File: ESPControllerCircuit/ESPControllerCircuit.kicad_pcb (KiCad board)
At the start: 2 copper layers, 5 parts, among them J1 Conn_01x02_Female, SW1 SW_Push, U1 WeMos_mini

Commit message: Basic controller circuit
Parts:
- removed J1: Conn_01x02_Female, Pin_Headers:Pin_Header_Straight_1x02_Pitch2.54mm
- added DEBUG1: Conn_01x02_Female, Pin_Headers:Pin_Header_Straight_1x02_Pitch2.54mm, F.Cu at (142.5, 137.8)
- added R2: 470R, Resistors_SMD:R_0805_HandSoldering, F.Cu at (131.8, 152.8)
- added R3: 220R, Resistors_SMD:R_0805_HandSoldering, F.Cu at (120.2, 152.8)
- added REF**: MountingHole_2.5mm, Mounting_Holes:MountingHole_2.5mm, F.Cu at (103.0, 110.0)
- added REF**: MountingHole_2.5mm, Mounting_Holes:MountingHole_2.5mm, F.Cu at (145.0, 110.0)
- added REF**: MountingHole_2.5mm, Mounting_Holes:MountingHole_2.5mm, F.Cu at (145.0, 64.0)
- added REF**: MountingHole_2.5mm, Mounting_Holes:MountingHole_2.5mm, F.Cu at (103.0, 64.0)
- added REF**: MountingHole_2.5mm, Mounting_Holes:MountingHole_2.5mm, F.Cu at (103.0, 157.0)
- added REF**: MountingHole_2.5mm, Mounting_Holes:MountingHole_2.5mm, F.Cu at (145.0, 157.0)
- added RX1: Conn_01x02_Male, Connectors_JST:JST_PH_S2B-PH-K_02x2.00mm_Angled, F.Cu at (137.0, 153.2)
- added TX1: Conn_01x02_Male, Connectors_JST:JST_PH_S2B-PH-K_02x2.00mm_Angled, F.Cu at (109.0, 153.2)
- added U2: HMHA2801, Housings_SSOP:SOP-4_4.4x2.8mm_Pitch1.27mm, F.Cu at (115.8, 155.5)
- D1: value LED -> COMMS
- R1: value 512R -> 470R
- moved R1 42.8 mm to (107.8, 147.0)
- moved D1 42.5 mm to (102.8, 147.0)
- moved U1 30.0 mm to (124.2, 132.2)
- moved SW1 19.4 mm to (145.5, 117.0), turned to 270 degrees
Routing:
- net +3V3: track 0.00 -> 33.1 mm
- net Net-(R2-Pad2): track 0.00 -> 31.8 mm
- net Net-(R3-Pad2): track 0.00 -> 17.8 mm
- net Net-(R1-Pad2): track 0.00 -> 15.8 mm
- net Net-(SW1-Pad2): track 0.00 -> 13.9 mm
- net Net-(TX1-Pad1): track 0.00 -> 8.99 mm
- net Net-(DEBUG1-Pad1): track 0.00 -> 8.12 mm
- net Net-(TX1-Pad2): track 0.00 -> 8.07 mm
- net Net-(R3-Pad1): track 0.00 -> 2.68 mm
- net Net-(D1-Pad2): track 0.00 -> 2.30 mm
- net GND: vias 0 -> 10
- added copper zone on B.Cu, net GND
- added copper zone on F.Cu, net GND
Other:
- board outline added: 48 x 99 mm

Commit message: End of day checkin
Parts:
- added R4: 10K, Resistors_SMD:R_0805_HandSoldering, F.Cu at (130.5, 128.2)
- added R5: 10K, Resistors_SMD:R_0805_HandSoldering, F.Cu at (130.5, 131.1)
- added U3: PCF8574AT/3 - I/O Expander, 8bit, 100 kHz, I2C, SMD_Packages:SO-16-W, F.Cu at (125.0, 118.8)
- R2: value 470R -> 4K7
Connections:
- U1 pad 11: Net-(U1-Pad11) -> Net-(R1-Pad2)
- U1 pad 12: Net-(U1-Pad12) -> PCFINT
- U1 pad 13: Net-(R1-Pad2) -> Net-(U1-Pad13)
- U1 pad 4: Net-(U1-Pad4) -> Net-(SW1-Pad2)
- U1 pad 5: Net-(U1-Pad5) -> SCL
- U1 pad 6: Net-(SW1-Pad2) -> SDA
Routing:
- net +3V3: track 33.1 -> 63.3 mm, vias 0 -> 1
- net SCL: track 0.00 -> 16.8 mm
- net PCFINT: track 0.00 -> 16.0 mm
- net SDA: track 0.00 -> 12.6 mm
- net Net-(R2-Pad2): track 31.8 -> 39.3 mm
- net Net-(SW1-Pad2): track 13.9 -> 20.8 mm
- net Net-(R1-Pad2): track 15.8 -> 21.6 mm
- net GND: track 0.00 -> 2.54 mm, vias 10 -> 20

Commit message: Got i2c working for PCF8574 chip
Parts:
- R4, R5: value 10K -> 4K7
- U3: value PCF8574AT/3 - I/O Expander, 8bit, 100 kHz, I2C -> PCF8574AT/3
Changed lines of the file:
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@@
       (effects (font (size 1 1) (thickness 0.15)))
     )
-    (fp_text value "PCF8574AT/3 -  I/O Expander, 8bit, 100 kHz, I2C" (at -39.75 3.75 180) (layer F.Fab)
+    (fp_text value PCF8574AT/3 (at -0.25 -2.75 180) (layer F.Fab)
       (effects (font (size 1 1) (thickness 0.15)))
     )
@@
       (effects (font (size 1 1) (thickness 0.15)))
     )
-    (fp_text value 10K (at 0 1.75) (layer F.Fab)
+    (fp_text value 4K7 (at 0 1.75) (layer F.Fab)
       (effects (font (size 1 1) (thickness 0.15)))
     )
@@
       (effects (font (size 1 1) (thickness 0.15)))
     )
-    (fp_text value 10K (at 0 1.75) (layer F.Fab)
+    (fp_text value 4K7 (at 0 1.75) (layer F.Fab)
       (effects (font (size 1 1) (thickness 0.15)))
     )
@@
       (effects (font (size 1 1) (thickness 0.15)))
     )
-    (fp_text value WeMos_mini (at 15.25 -7.75) (layer F.Fab)
-      (effects (font (size 1 1) (thickness 0.15)))
-    )
+    (fp_text value WeMos_mini (at -2.25 -8.25 90) (layer F.Fab)
+      (effects (font (size 1 1) (thickness 0.15)))
+    )

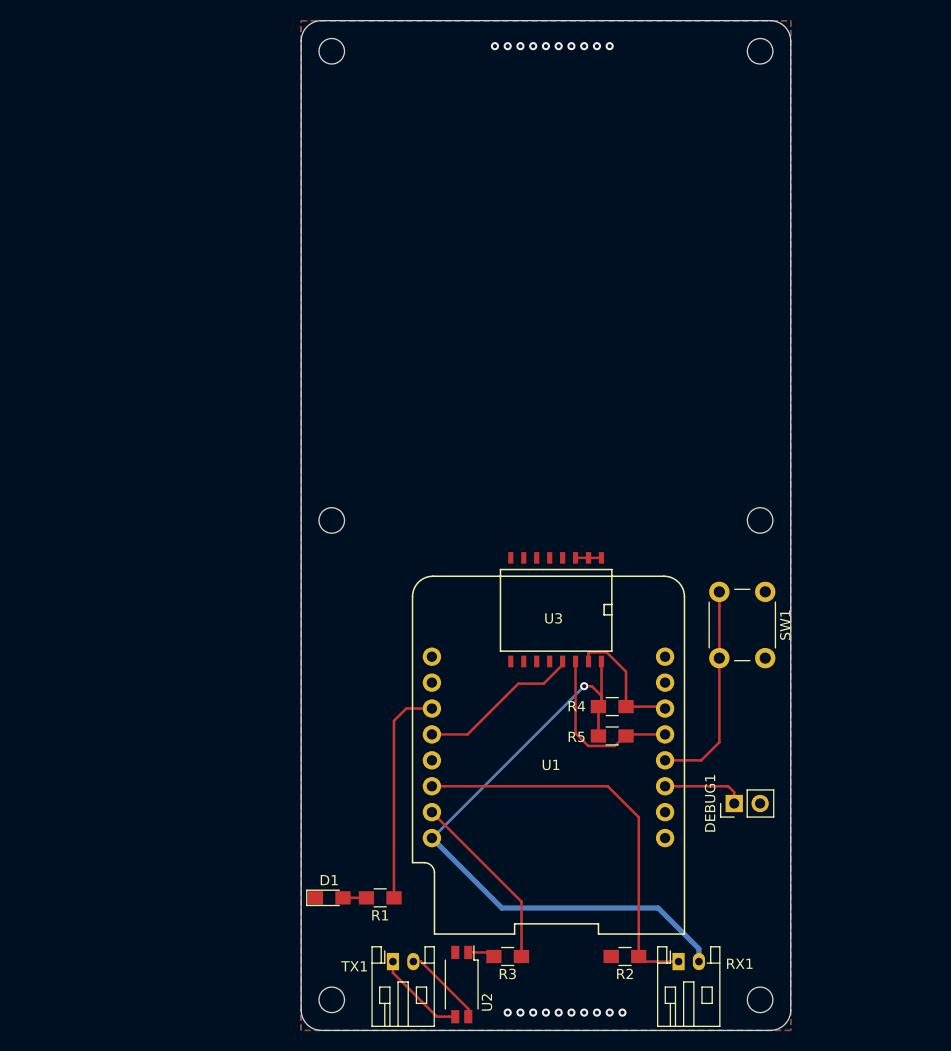
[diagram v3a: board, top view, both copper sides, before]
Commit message: Controller module PCB design
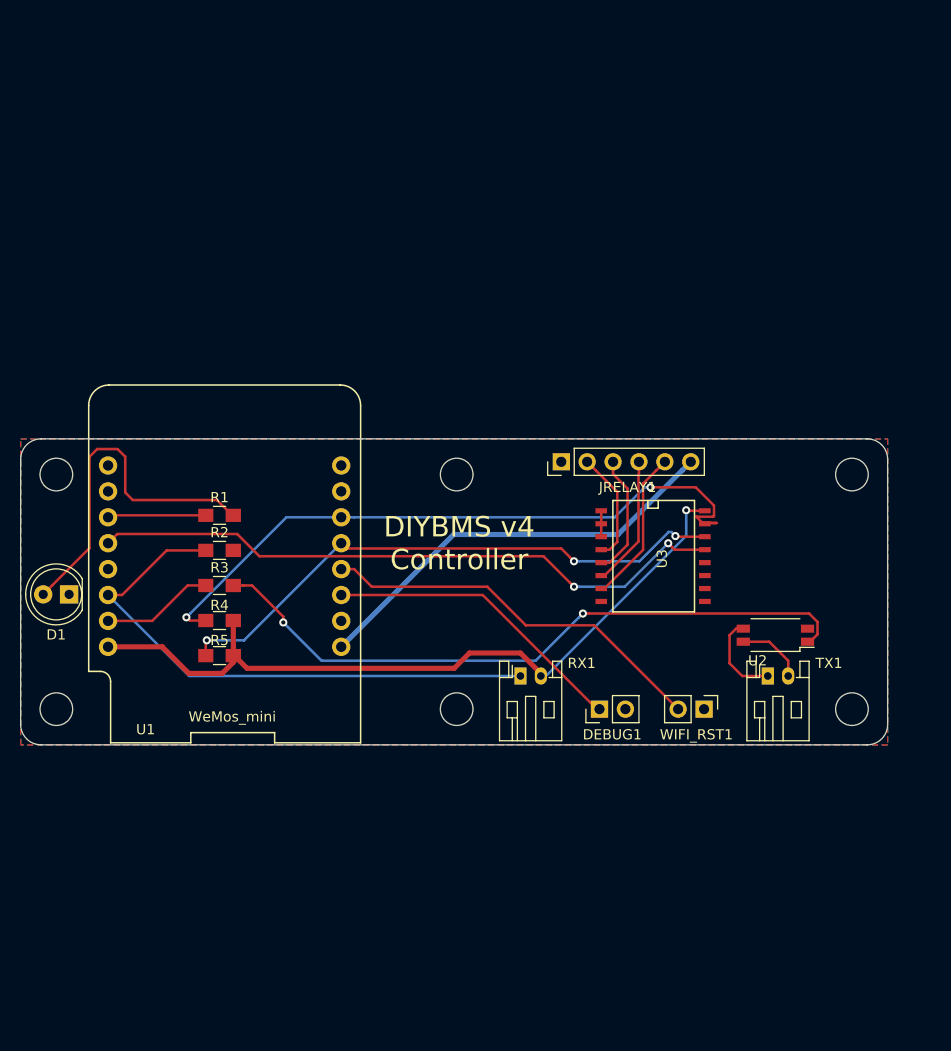
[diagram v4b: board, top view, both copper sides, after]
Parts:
- removed the REF** at (103.0, 110.0)
- removed the REF** at (145.0, 110.0)
- removed the REF** at (145.0, 64.0)
- removed the REF** at (103.0, 64.0)
- removed the REF** at (103.0, 157.0)
- removed the REF** at (145.0, 157.0)
- removed SW1: SW_Push, Buttons_Switches_THT:SW_PUSH_6mm
- added JRELAY1: Conn_01x06_Male, Pin_Headers:Pin_Header_Straight_1x06_Pitch2.54mm, F.Cu at (125.5, 104.2)
- added REF**: MountingHole_3.2mm_M3, Mounting_Holes:MountingHole_3.2mm_M3, F.Cu at (115.2, 128.5)
- added REF**: MountingHole_3.2mm_M3, Mounting_Holes:MountingHole_3.2mm_M3, F.Cu at (115.2, 105.5)
- added REF**: MountingHole_3.2mm_M3, Mounting_Holes:MountingHole_3.2mm_M3, F.Cu at (76.0, 105.5)
- added REF**: MountingHole_3.2mm_M3, Mounting_Holes:MountingHole_3.2mm_M3, F.Cu at (76.0, 128.5)
- added REF**: MountingHole_3.2mm_M3, Mounting_Holes:MountingHole_3.2mm_M3, F.Cu at (154.0, 128.5)
- added REF**: MountingHole_3.2mm_M3, Mounting_Holes:MountingHole_3.2mm_M3, F.Cu at (154.0, 105.5)
- added WIFI_RST1: WIFI RST, Pin_Headers:Pin_Header_Straight_1x02_Pitch2.54mm, F.Cu at (139.5, 128.5)
- D1: footprint LEDs:LED_0805_HandSoldering -> LEDs:LED_D5.0mm
- moved R2 56.3 mm to (92.0, 112.9), turned to 180 degrees
- moved TX1 46.2 mm to (145.8, 125.2)
- moved R3 46.1 mm to (92.0, 116.4), turned to 180 degrees
- moved U2 46.0 mm to (146.5, 121.2), turned to 180 degrees
- moved R1 40.7 mm to (92.0, 109.5), turned to 180 degrees
- moved R4 39.4 mm to (92.0, 119.8), turned to 180 degrees
- moved R5 39.3 mm to (92.0, 123.2), turned to 180 degrees
- moved D1 39.2 mm to (77.2, 117.2), turned to 180 degrees
- moved U1 36.9 mm to (92.5, 113.5)
- moved RX1 32.0 mm to (121.5, 125.2)
- moved DEBUG1 16.1 mm to (129.2, 128.5)
- moved U3 10.9 mm to (134.5, 113.5), turned to 270 degrees
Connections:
- U1 pad 10: Net-(U1-Pad10) -> (no net)
- U1 pad 13: Net-(U1-Pad13) -> (no net)
- U1 pad 7: Net-(U1-Pad7) -> (no net)
- U1 pad 8: Net-(U1-Pad8) -> (no net)
- U1 pad 9: Net-(U1-Pad9) -> (no net)
- U3 pad 10: Net-(U3-Pad10) -> (no net)
- U3 pad 11: Net-(U3-Pad11) -> (no net)
- U3 pad 12: Net-(U3-Pad12) -> (no net)
- U3 pad 9: Net-(U3-Pad9) -> (no net)
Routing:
- net Net-(R3-Pad1): track 2.68 -> 65.4 mm, vias 0 -> 2
- net SDA: track 12.6 -> 66.0 mm, vias 0 -> 2
- net PCFINT: track 16.0 -> 63.0 mm, vias 0 -> 2
- net +5V: track 0.00 -> 41.8 mm
- net SCL: track 16.8 -> 56.4 mm, vias 0 -> 3
- net Net-(D1-Pad2): track 2.30 -> 34.5 mm
- net Net-(DEBUG1-Pad1): track 8.12 -> 30.0 mm
- net Net-(U1-Pad4): track 20.8 -> 38.7 mm
- net Net-(R2-Pad2): track 39.3 -> 55.1 mm
- net Net-(JRELAY1-Pad5): track 0.00 -> 15.2 mm
- net Net-(JRELAY1-Pad4): track 0.00 -> 12.9 mm
- net Net-(JRELAY1-Pad3): track 0.00 -> 12.0 mm
- net Net-(R1-Pad2): track 21.6 -> 9.66 mm
- net +3V3: track 63.3 -> 74.6 mm
- net Net-(JRELAY1-Pad2): track 0.00 -> 11.0 mm
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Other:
- board size 48 x 99 mm -> 85 x 30 mm
- board text added: "22 May 2019"
- board text added: "DIYBMS v4 Controller"
- board text added: "github.com/stuartpittaway/diyBMSv4"
- board text added: "©2019 Stuart Pittaway"

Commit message: COntroller updates
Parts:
- moved R1 16.1 mm to (76.0, 111.2)
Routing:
- net Net-(D1-Pad2): track 34.5 -> 7.09 mm
- net +5V: track 41.8 -> 47.9 mm
- net PCFINT: track 63.0 -> 67.4 mm
- net SDA: track 66.0 -> 62.3 mm
- net Net-(R1-Pad2): track 9.66 -> 7.07 mm
- net GND: vias 0 -> 4
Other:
- board text added: "+"
- board text added: "1"
- board text added: "3V3"
- board text added: "5V"
- board text added: "D3"
- board text added: "DEBUG"
- board text added: "GND"
- board text added: "SCL"
- board text added: "SDA"

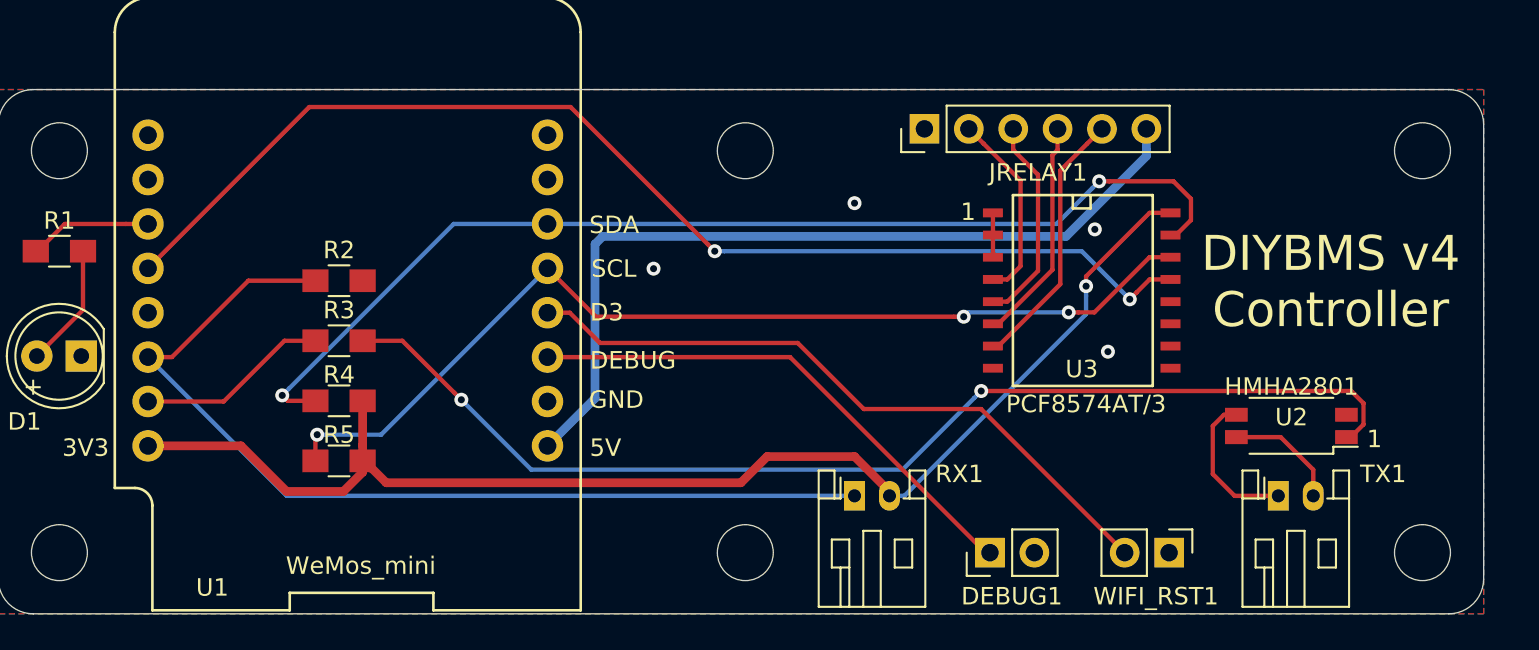
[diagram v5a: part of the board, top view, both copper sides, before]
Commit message: Updated controller module circuit and test of PCF8574
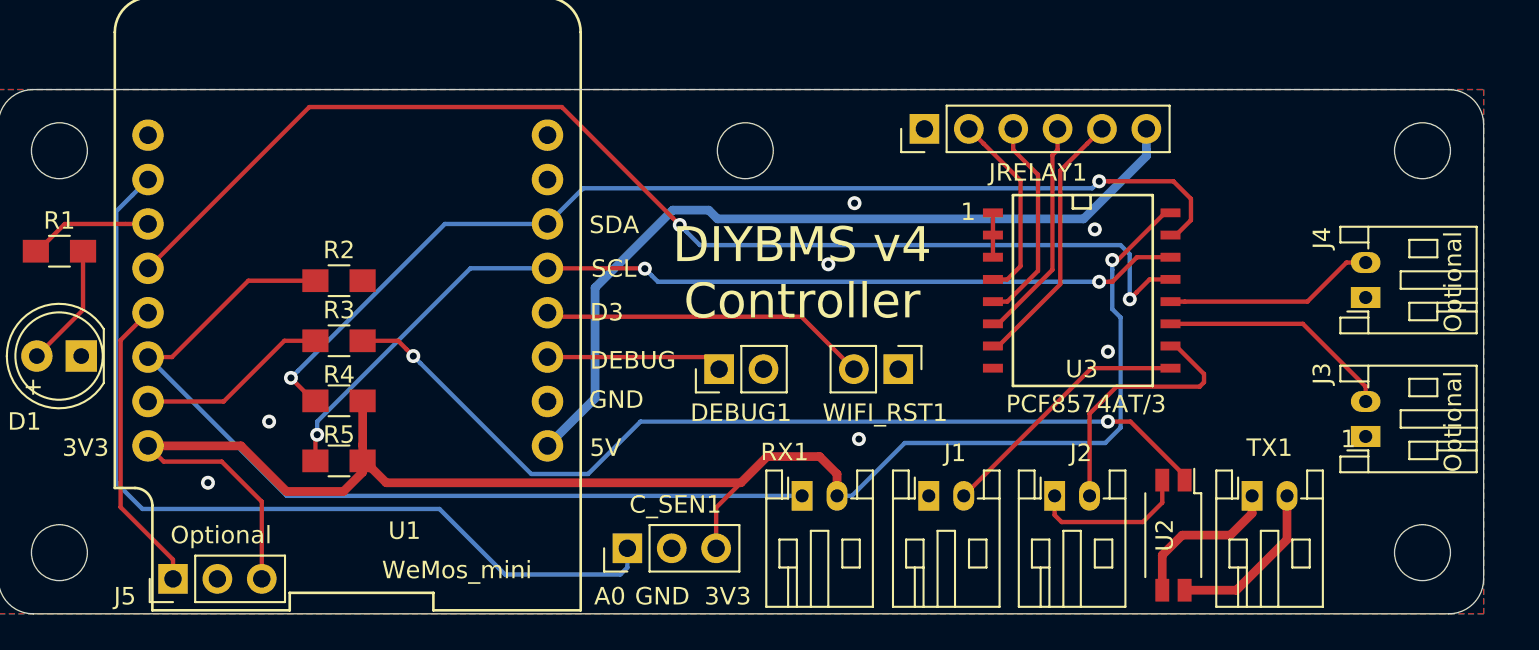
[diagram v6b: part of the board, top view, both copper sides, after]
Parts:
- removed the REF** at (115.2, 128.5)
- added C_SEN1: Current Sensor, Pin_Headers:Pin_Header_Straight_1x03_Pitch2.54mm, F.Cu at (108.5, 128.2)
- added J1: Input, Connectors_JST:JST_PH_S2B-PH-K_02x2.00mm_Angled, F.Cu at (125.8, 125.2)
- added J2: Input, Connectors_JST:JST_PH_S2B-PH-K_02x2.00mm_Angled, F.Cu at (132.9, 125.2)
- added J3: Input, Connectors_JST:JST_PH_S2B-PH-K_02x2.00mm_Angled, F.Cu at (150.8, 121.8)
- added J4: Input, Connectors_JST:JST_PH_S2B-PH-K_02x2.00mm_Angled, F.Cu at (150.8, 113.9)
- added J5: Optional, Pin_Headers:Pin_Header_Straight_1x03_Pitch2.54mm, F.Cu at (82.5, 130.0)
- RX1: value Conn_01x02_Male -> Receive
- TX1: value Conn_01x02_Male -> Transmit
- moved DEBUG1 18.7 mm to (113.8, 118.0)
- moved WIFI_RST1 18.7 mm to (124.0, 118.0)
- moved U2 9.20 mm to (139.8, 127.5), turned to 270 degrees
- moved RX1 3.00 mm to (118.5, 125.2)
- moved TX1 1.50 mm to (144.2, 125.2)
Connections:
- U1 pad 10: (no net) -> Net-(C_SEN1-Pad1)
- U1 pad 13: (no net) -> Net-(J5-Pad1)
- U3 pad 10: (no net) -> Net-(J2-Pad2)
- U3 pad 11: (no net) -> Net-(J3-Pad2)
- U3 pad 12: (no net) -> Net-(J4-Pad2)
- U3 pad 9: (no net) -> Net-(J1-Pad2)
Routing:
- net Net-(C_SEN1-Pad1): track 0.00 -> 50.8 mm
- net +3V3: track 74.3 -> 98.7 mm
- net Net-(U1-Pad4): track 38.7 -> 18.9 mm
- net Net-(DEBUG1-Pad1): track 30.0 -> 10.1 mm
- net Net-(J5-Pad1): track 0.00 -> 17.1 mm
- net Net-(J2-Pad2): track 0.00 -> 15.1 mm
- net Net-(J1-Pad2): track 0.00 -> 14.9 mm
- net Net-(J3-Pad2): track 0.00 -> 13.5 mm
- net Net-(J4-Pad2): track 0.00 -> 12.1 mm
- net Net-(R3-Pad1): track 65.0 -> 53.0 mm
- net GND: track 2.54 -> 11.7 mm, vias 4 -> 7
- net Net-(R2-Pad2): track 55.1 -> 52.1 mm
- net Net-(TX1-Pad2): track 6.67 -> 9.56 mm
- net PCFINT: track 67.4 -> 68.9 mm
- net SCL: track 56.9 -> 55.7 mm
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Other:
- board text added: "A0"
- board text added: "Optional"
